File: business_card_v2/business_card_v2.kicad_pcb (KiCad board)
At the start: 2 copper layers, 85.6 x 54 mm, 12 parts, among them M1 CH32X035F7P6, U1 CH32V006F8P6, U10 CH32V006F8P6, U2 CH32V006F8P6, U3 CH32V006F8P6, U4 CH32V006F8P6, U5 CH32V006F8P6, U6 CH32V006F8P6, U7 CH32V006F8P6, U8 CH32V006F8P6, U9 CH32V006F8P6

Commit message: bottom left to top right pins
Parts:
- removed U10: CH32V006F8P6, Package_SO:TSSOP-20_4.4x6.5mm_P0.65mm
- added C1: 100nF, Capacitor_SMD:C_0603_1608Metric, B.Cu at (58.2, 120.0)
- added C10: 10uF, Capacitor_SMD:C_0603_1608Metric, B.Cu at (62.2, 127.5)
- added C11: 100nF, Capacitor_SMD:C_0603_1608Metric, B.Cu at (62.2, 130.0)
- added C12: 100nF, Capacitor_SMD:C_0603_1608Metric, B.Cu at (62.2, 132.5)
- added C13: 100nF, Capacitor_SMD:C_0603_1608Metric, B.Cu at (66.2, 120.0)
- added C14: 100nF, Capacitor_SMD:C_0603_1608Metric, B.Cu at (66.2, 122.5)
- added C15: 100nF, Capacitor_SMD:C_0603_1608Metric, B.Cu at (66.2, 125.0)
- added C16: 100nF, Capacitor_SMD:C_0603_1608Metric, B.Cu at (66.2, 127.5)
- added C17: 100nF, Capacitor_SMD:C_0603_1608Metric, B.Cu at (66.2, 130.0)
- added C18: 100nF, Capacitor_SMD:C_0603_1608Metric, B.Cu at (66.2, 132.5)
- added C19: 100nF, Capacitor_SMD:C_0603_1608Metric, B.Cu at (70.2, 120.0)
- added C2: 100nF, Capacitor_SMD:C_0603_1608Metric, B.Cu at (58.2, 122.5)
- added C20: 100nF, Capacitor_SMD:C_0603_1608Metric, B.Cu at (70.2, 122.5)
- added C21: 100nF, Capacitor_SMD:C_0603_1608Metric, B.Cu at (70.2, 125.0)
- added C22: 100nF, Capacitor_SMD:C_0603_1608Metric, B.Cu at (51.9, 66.7)
- added C23: 100nF, Capacitor_SMD:C_0603_1608Metric, B.Cu at (52.6, 69.1)
- added C26: 100nF, Capacitor_SMD:C_0603_1608Metric, B.Cu at (70.2, 132.5)
- added C3: 100nF, Capacitor_SMD:C_0603_1608Metric, B.Cu at (58.2, 125.0)
- added C4: 100nF, Capacitor_SMD:C_0603_1608Metric, B.Cu at (58.2, 127.5)
- added C5: 100nF, Capacitor_SMD:C_0603_1608Metric, B.Cu at (58.2, 130.0)
- added C6: 100nF, Capacitor_SMD:C_0603_1608Metric, B.Cu at (58.2, 132.5)
- added C7: 10uF, Capacitor_SMD:C_0603_1608Metric, B.Cu at (62.2, 120.0)
- added C8: 100nF, Capacitor_SMD:C_0603_1608Metric, B.Cu at (62.2, 122.5)
- added C9: 100nF, Capacitor_SMD:C_0603_1608Metric, B.Cu at (62.2, 125.0)
- added D1: LED, LED_SMD:LED_1206_3216Metric, B.Cu at (167.9, 126.0)
- added D2: LED, LED_SMD:LED_1206_3216Metric, B.Cu at (168.0, 122.6)
- added D3: LED, LED_SMD:LED_1206_3216Metric, B.Cu at (168.0, 119.2)
- added D4: LED, LED_SMD:LED_1206_3216Metric, B.Cu at (168.0, 115.8)
- added D5: LED, LED_SMD:LED_1206_3216Metric, B.Cu at (168.0, 112.4)
- added D6: LED, LED_SMD:LED_1206_3216Metric, B.Cu at (168.0, 109.0)
- added D7: LED, LED_SMD:LED_1206_3216Metric, B.Cu at (168.0, 105.6)
- added D8: LED, LED_SMD:LED_1206_3216Metric, B.Cu at (168.0, 102.2)
- added D9: LED, LED_SMD:LED_1206_3216Metric, B.Cu at (39.4, 67.7)
- added G***: LOGO, Silkscreen:silkscreen_front_2, F.Cu at (76.9, 65.6)
- added P1: AMS1117-3.3, Package_TO_SOT_SMD:SOT-223-3_TabPin2, B.Cu at (146.9, 100.8)
- added R10: 1k, Resistor_SMD:R_0603_1608Metric, B.Cu at (151.4, 107.8)
- added R11: 1k, Resistor_SMD:R_0603_1608Metric, B.Cu at (41.0, 64.7)
- added R2: 10k, Resistor_SMD:R_0603_1608Metric, B.Cu at (143.9, 111.8)
- added R3: 1k, Resistor_SMD:R_0603_1608Metric, B.Cu at (146.4, 111.8)
- added R4: 1k, Resistor_SMD:R_0603_1608Metric, B.Cu at (148.9, 111.8)
- added R5: 1k, Resistor_SMD:R_0603_1608Metric, B.Cu at (151.4, 111.8)
- added R6: 1k, Resistor_SMD:R_0603_1608Metric, B.Cu at (154.5, 111.8)
- added R7: 1k, Resistor_SMD:R_0603_1608Metric, B.Cu at (143.9, 107.8)
- added R8: 1k, Resistor_SMD:R_0603_1608Metric, B.Cu at (146.4, 107.8)
- added R9: 1k, Resistor_SMD:R_0603_1608Metric, B.Cu at (148.9, 107.8)
- added S1_GP0: ~, TestPoint:TestPoint_Pad_D1.0mm, B.Cu at (111.8, 74.9)
- added S1_GP1: ~, TestPoint:TestPoint_Pad_D1.0mm, B.Cu at (112.4, 77.5)
- added S1_GP10: ~, TestPoint:TestPoint_Pad_D1.0mm, B.Cu at (111.1, 82.5)
- added S1_GP11: ~, TestPoint:TestPoint_Pad_D1.0mm, B.Cu at (110.5, 80.0)
- added S1_GP12: ~, TestPoint:TestPoint_Pad_D1.0mm, B.Cu at (109.9, 77.5)
- added S1_GP13: ~, TestPoint:TestPoint_Pad_D1.0mm, B.Cu at (109.2, 74.9)
- added S1_GP2: ~, TestPoint:TestPoint_Pad_D1.0mm, B.Cu at (113.0, 80.0)
- added S1_GP3: ~, TestPoint:TestPoint_Pad_D1.0mm, B.Cu at (113.7, 82.5)
- added S1_GP4: ~, TestPoint:TestPoint_Pad_D1.0mm, B.Cu at (114.3, 85.1)
- added S1_GP5: ~, TestPoint:TestPoint_Pad_D1.0mm, B.Cu at (114.9, 87.6)
- added S1_GP6: ~, TestPoint:TestPoint_Pad_D1.0mm, B.Cu at (115.6, 90.2)
- added S1_GP7: ~, TestPoint:TestPoint_Pad_D1.0mm, B.Cu at (113.0, 90.2)
- added S1_GP8: ~, TestPoint:TestPoint_Pad_D1.0mm, B.Cu at (112.4, 87.6)
- added S1_GP9: ~, TestPoint:TestPoint_Pad_D1.0mm, B.Cu at (111.8, 85.1)
- added S2_GP0: ~, TestPoint:TestPoint_Pad_D1.0mm, B.Cu at (103.5, 74.9)
- added S2_GP1: ~, TestPoint:TestPoint_Pad_D1.0mm, B.Cu at (104.1, 77.5)
- added S2_GP10: ~, TestPoint:TestPoint_Pad_D1.0mm, B.Cu at (102.9, 82.5)
- added S2_GP11: ~, TestPoint:TestPoint_Pad_D1.0mm, B.Cu at (102.2, 80.0)
- added S2_GP12: ~, TestPoint:TestPoint_Pad_D1.0mm, B.Cu at (101.6, 77.5)
- added S2_GP13: ~, TestPoint:TestPoint_Pad_D1.0mm, B.Cu at (101.0, 74.9)
- added S2_GP2: ~, TestPoint:TestPoint_Pad_D1.0mm, B.Cu at (104.8, 80.0)
- added S2_GP3: ~, TestPoint:TestPoint_Pad_D1.0mm, B.Cu at (105.4, 82.5)
- added S2_GP4: ~, TestPoint:TestPoint_Pad_D1.0mm, B.Cu at (106.0, 85.1)
- added S2_GP5: ~, TestPoint:TestPoint_Pad_D1.0mm, B.Cu at (106.7, 87.6)
- added S2_GP6: ~, TestPoint:TestPoint_Pad_D1.0mm, B.Cu at (107.3, 90.1)
- added S2_GP7: ~, TestPoint:TestPoint_Pad_D1.0mm, B.Cu at (104.8, 90.2)
- added S2_GP8: ~, TestPoint:TestPoint_Pad_D1.0mm, B.Cu at (104.1, 87.6)
- added S2_GP9: ~, TestPoint:TestPoint_Pad_D1.0mm, B.Cu at (103.5, 85.1)
- added S3_GP0: ~, TestPoint:TestPoint_Pad_D1.0mm, B.Cu at (94.6, 74.9)
- added S3_GP1: ~, TestPoint:TestPoint_Pad_D1.0mm, B.Cu at (95.2, 77.5)
- added S3_GP10: ~, TestPoint:TestPoint_Pad_D1.0mm, B.Cu at (94.0, 82.5)
- added S3_GP11: ~, TestPoint:TestPoint_Pad_D1.0mm, B.Cu at (93.3, 80.0)
- added S3_GP12: ~, TestPoint:TestPoint_Pad_D1.0mm, B.Cu at (92.7, 77.5)
- added S3_GP13: ~, TestPoint:TestPoint_Pad_D1.0mm, B.Cu at (92.1, 74.9)
- added S3_GP2: ~, TestPoint:TestPoint_Pad_D1.0mm, B.Cu at (95.9, 80.0)
- added S3_GP3: ~, TestPoint:TestPoint_Pad_D1.0mm, B.Cu at (96.5, 82.5)
- added S3_GP4: ~, TestPoint:TestPoint_Pad_D1.0mm, B.Cu at (97.2, 85.1)
- added S3_GP5: ~, TestPoint:TestPoint_Pad_D1.0mm, B.Cu at (97.8, 87.6)
- added S3_GP6: ~, TestPoint:TestPoint_Pad_D1.0mm, B.Cu at (98.4, 90.2)
- added S3_GP7: ~, TestPoint:TestPoint_Pad_D1.0mm, B.Cu at (95.9, 90.2)
- added S3_GP8: ~, TestPoint:TestPoint_Pad_D1.0mm, B.Cu at (95.2, 87.6)
- added S3_GP9: ~, TestPoint:TestPoint_Pad_D1.0mm, B.Cu at (94.6, 85.1)
- added S4_GP0: ~, TestPoint:TestPoint_Pad_D1.0mm, B.Cu at (85.7, 74.9)
- added S4_GP1: ~, TestPoint:TestPoint_Pad_D1.0mm, B.Cu at (86.4, 77.5)
- added S4_GP10: ~, TestPoint:TestPoint_Pad_D1.0mm, B.Cu at (85.1, 82.5)
- added S4_GP11: ~, TestPoint:TestPoint_Pad_D1.0mm, B.Cu at (84.5, 80.0)
- added S4_GP12: ~, TestPoint:TestPoint_Pad_D1.0mm, B.Cu at (83.8, 77.5)
- added S4_GP13: ~, TestPoint:TestPoint_Pad_D1.0mm, B.Cu at (83.2, 74.9)
- added S4_GP2: ~, TestPoint:TestPoint_Pad_D1.0mm, B.Cu at (87.0, 80.0)
- added S4_GP3: ~, TestPoint:TestPoint_Pad_D1.0mm, B.Cu at (87.6, 82.6)
- added S4_GP4: ~, TestPoint:TestPoint_Pad_D1.0mm, B.Cu at (88.3, 85.1)
- added S4_GP5: ~, TestPoint:TestPoint_Pad_D1.0mm, B.Cu at (88.9, 87.7)
- added S4_GP6: ~, TestPoint:TestPoint_Pad_D1.0mm, B.Cu at (89.5, 90.2)
- added S4_GP7: ~, TestPoint:TestPoint_Pad_D1.0mm, B.Cu at (87.0, 90.2)
- added S4_GP8: ~, TestPoint:TestPoint_Pad_D1.0mm, B.Cu at (86.4, 87.6)
- added S4_GP9: ~, TestPoint:TestPoint_Pad_D1.0mm, B.Cu at (85.7, 85.1)
- added S5_GP0: ~, TestPoint:TestPoint_Pad_D1.0mm, B.Cu at (76.8, 74.9)
- added S5_GP1: ~, TestPoint:TestPoint_Pad_D1.0mm, B.Cu at (77.5, 77.5)
- added S5_GP10: ~, TestPoint:TestPoint_Pad_D1.0mm, B.Cu at (76.2, 82.5)
- added S5_GP11: ~, TestPoint:TestPoint_Pad_D1.0mm, B.Cu at (75.6, 80.0)
- added S5_GP12: ~, TestPoint:TestPoint_Pad_D1.0mm, B.Cu at (74.9, 77.5)
- added S5_GP13: ~, TestPoint:TestPoint_Pad_D1.0mm, B.Cu at (74.3, 74.9)
- added S5_GP2: ~, TestPoint:TestPoint_Pad_D1.0mm, B.Cu at (78.1, 80.0)
- added S5_GP3: ~, TestPoint:TestPoint_Pad_D1.0mm, B.Cu at (78.7, 82.5)
- added S5_GP4: ~, TestPoint:TestPoint_Pad_D1.0mm, B.Cu at (79.4, 85.1)
- added S5_GP5: ~, TestPoint:TestPoint_Pad_D1.0mm, B.Cu at (80.0, 87.6)
- added S5_GP6: ~, TestPoint:TestPoint_Pad_D1.0mm, B.Cu at (80.6, 90.2)
- added S5_GP7: ~, TestPoint:TestPoint_Pad_D1.0mm, B.Cu at (78.1, 90.2)
- added S5_GP8: ~, TestPoint:TestPoint_Pad_D1.0mm, B.Cu at (77.5, 87.6)
- added S5_GP9: ~, TestPoint:TestPoint_Pad_D1.0mm, B.Cu at (76.8, 85.1)
- added S6_GP0: ~, TestPoint:TestPoint_Pad_D1.0mm, B.Cu at (67.9, 74.9)
- added S6_GP1: ~, TestPoint:TestPoint_Pad_D1.0mm, B.Cu at (68.6, 77.5)
- added S6_GP10: ~, TestPoint:TestPoint_Pad_D1.0mm, B.Cu at (67.3, 82.5)
- added S6_GP11: ~, TestPoint:TestPoint_Pad_D1.0mm, B.Cu at (66.7, 80.0)
- added S6_GP12: ~, TestPoint:TestPoint_Pad_D1.0mm, B.Cu at (66.0, 77.5)
- added S6_GP13: ~, TestPoint:TestPoint_Pad_D1.0mm, B.Cu at (65.4, 74.9)
- added S6_GP2: ~, TestPoint:TestPoint_Pad_D1.0mm, B.Cu at (69.2, 80.0)
- added S6_GP3: ~, TestPoint:TestPoint_Pad_D1.0mm, B.Cu at (69.8, 82.5)
- added S6_GP4: ~, TestPoint:TestPoint_Pad_D1.0mm, B.Cu at (70.5, 85.1)
- added S6_GP5: ~, TestPoint:TestPoint_Pad_D1.0mm, B.Cu at (71.1, 87.6)
- added S6_GP6: ~, TestPoint:TestPoint_Pad_D1.0mm, B.Cu at (71.8, 90.2)
- added S6_GP7: ~, TestPoint:TestPoint_Pad_D1.0mm, B.Cu at (69.2, 90.2)
- added S6_GP8: ~, TestPoint:TestPoint_Pad_D1.0mm, B.Cu at (68.6, 87.6)
- added S6_GP9: ~, TestPoint:TestPoint_Pad_D1.0mm, B.Cu at (67.9, 85.1)
- added S7_GP0: ~, TestPoint:TestPoint_Pad_D1.0mm, B.Cu at (59.1, 74.9)
- added S7_GP1: ~, TestPoint:TestPoint_Pad_D1.0mm, B.Cu at (59.7, 77.5)
- added S7_GP10: ~, TestPoint:TestPoint_Pad_D1.0mm, B.Cu at (58.4, 82.5)
- added S7_GP11: ~, TestPoint:TestPoint_Pad_D1.0mm, B.Cu at (57.8, 80.0)
- added S7_GP12: ~, TestPoint:TestPoint_Pad_D1.0mm, B.Cu at (57.1, 77.5)
- added S7_GP13: ~, TestPoint:TestPoint_Pad_D1.0mm, B.Cu at (56.5, 74.9)
- added S7_GP2: ~, TestPoint:TestPoint_Pad_D1.0mm, B.Cu at (61.6, 85.1)
- added S7_GP3: ~, TestPoint:TestPoint_Pad_D1.0mm, B.Cu at (60.3, 80.0)
- added S7_GP4: ~, TestPoint:TestPoint_Pad_D1.0mm, B.Cu at (61.0, 82.5)
- added S7_GP5: ~, TestPoint:TestPoint_Pad_D1.0mm, B.Cu at (62.2, 87.6)
- added S7_GP6: ~, TestPoint:TestPoint_Pad_D1.0mm, B.Cu at (62.9, 90.2)
- added S7_GP7: ~, TestPoint:TestPoint_Pad_D1.0mm, B.Cu at (60.3, 90.2)
- added S7_GP8: ~, TestPoint:TestPoint_Pad_D1.0mm, B.Cu at (59.7, 87.6)
- added S7_GP9: ~, TestPoint:TestPoint_Pad_D1.0mm, B.Cu at (59.1, 85.1)
- added S8_GP0: ~, TestPoint:TestPoint_Pad_D1.0mm, B.Cu at (50.2, 74.9)
- added S8_GP1: ~, TestPoint:TestPoint_Pad_D1.0mm, B.Cu at (50.8, 77.5)
- added S8_GP10: ~, TestPoint:TestPoint_Pad_D1.0mm, B.Cu at (49.5, 82.5)
- added S8_GP11: ~, TestPoint:TestPoint_Pad_D1.0mm, B.Cu at (48.9, 80.0)
- added S8_GP12: ~, TestPoint:TestPoint_Pad_D1.0mm, B.Cu at (48.3, 77.5)
- added S8_GP13: ~, TestPoint:TestPoint_Pad_D1.0mm, B.Cu at (47.6, 74.9)
- added S8_GP2: ~, TestPoint:TestPoint_Pad_D1.0mm, B.Cu at (51.4, 80.0)
- added S8_GP3: ~, TestPoint:TestPoint_Pad_D1.0mm, B.Cu at (52.1, 82.5)
- added S8_GP4: ~, TestPoint:TestPoint_Pad_D1.0mm, B.Cu at (52.7, 85.1)
- added S8_GP5: ~, TestPoint:TestPoint_Pad_D1.0mm, B.Cu at (53.3, 87.6)
- added S8_GP6: ~, TestPoint:TestPoint_Pad_D1.0mm, B.Cu at (54.0, 90.2)
- added S8_GP7: ~, TestPoint:TestPoint_Pad_D1.0mm, B.Cu at (51.4, 90.2)
- added S8_GP8: ~, TestPoint:TestPoint_Pad_D1.0mm, B.Cu at (50.8, 87.6)
- added S8_GP9: ~, TestPoint:TestPoint_Pad_D1.0mm, B.Cu at (50.2, 85.1)
- added S9_GP0: ~, TestPoint:TestPoint_Pad_D1.0mm, B.Cu at (41.3, 74.9)
- added S9_GP1: ~, TestPoint:TestPoint_Pad_D1.0mm, B.Cu at (41.9, 77.5)
- added S9_GP10: ~, TestPoint:TestPoint_Pad_D1.0mm, B.Cu at (40.6, 82.5)
- added S9_GP11: ~, TestPoint:TestPoint_Pad_D1.0mm, B.Cu at (40.0, 80.0)
- added S9_GP12: ~, TestPoint:TestPoint_Pad_D1.0mm, B.Cu at (39.4, 77.5)
- added S9_GP13: ~, TestPoint:TestPoint_Pad_D1.0mm, B.Cu at (38.7, 74.9)
- added S9_GP2: ~, TestPoint:TestPoint_Pad_D1.0mm, B.Cu at (42.5, 80.0)
- added S9_GP3: ~, TestPoint:TestPoint_Pad_D1.0mm, B.Cu at (43.2, 82.5)
- added S9_GP4: ~, TestPoint:TestPoint_Pad_D1.0mm, B.Cu at (43.8, 85.1)
- added S9_GP5: ~, TestPoint:TestPoint_Pad_D1.0mm, B.Cu at (44.5, 87.6)
- added S9_GP6: ~, TestPoint:TestPoint_Pad_D1.0mm, B.Cu at (45.1, 90.2)
- added S9_GP7: ~, TestPoint:TestPoint_Pad_D1.0mm, B.Cu at (42.5, 90.2)
- added S9_GP8: ~, TestPoint:TestPoint_Pad_D1.0mm, B.Cu at (41.9, 87.6)
- added S9_GP9: ~, TestPoint:TestPoint_Pad_D1.0mm, B.Cu at (41.3, 85.1)
- added SW3: SW_Push, Button_Switch_SMD:SW_SPST_TL3342, B.Cu at (154.5, 101.0)
- added TP1: SWIO_N1, TestPoint:TestPoint_Pad_D2.0mm, B.Cu at (116.8, 67.3)
- added TP11: SWDIO_M, TestPoint:TestPoint_Pad_D2.0mm, B.Cu at (113.7, 59.7)
- added TP12: SWCLK_M, TestPoint:TestPoint_Pad_D2.0mm, B.Cu at (113.7, 63.5)
- added TP13: GND, TestPoint:TestPoint_Pad_D2.0mm, B.Cu at (116.8, 59.7)
- added TP14: BUS_MOSI, TestPoint:TestPoint_Pad_D2.0mm, B.Cu at (110.5, 59.7)
- added TP15: BUS_MISO, TestPoint:TestPoint_Pad_D2.0mm, B.Cu at (110.5, 63.5)
- added TP2: SWIO_N2, TestPoint:TestPoint_Pad_D2.0mm, B.Cu at (116.8, 71.1)
- added TP3: SWIO_N3, TestPoint:TestPoint_Pad_D2.0mm, B.Cu at (113.7, 67.3)
- added TP4: SWIO_N4, TestPoint:TestPoint_Pad_D2.0mm, B.Cu at (113.7, 71.1)
- added TP5: SWIO_N5, TestPoint:TestPoint_Pad_D2.0mm, B.Cu at (110.5, 67.3)
- added TP6: SWIO_N6, TestPoint:TestPoint_Pad_D2.0mm, B.Cu at (110.5, 71.1)
- added TP7: SWIO_N7, TestPoint:TestPoint_Pad_D2.0mm, B.Cu at (107.3, 67.3)
- added TP8: SWIO_N8, TestPoint:TestPoint_Pad_D2.0mm, B.Cu at (107.3, 71.1)
- added TP9: SWIO_N9, TestPoint:TestPoint_Pad_D2.0mm, B.Cu at (116.8, 74.9)
- M1, U1, U2, U3, U4, U5, U6, U7, U8, U9: moved to B.Cu
- moved U7 48.1 mm to (46.4, 44.5), turned to 180 degrees
- moved U9 44.4 mm to (46.4, 67.3), turned to 180 degrees
- moved U8 44.1 mm to (46.4, 55.9), turned to 180 degrees
- moved M1 34.6 mm to (106.5, 49.5)
- moved J1 27.0 mm to (113.4, 50.8)
- moved U1 23.2 mm to (95.2, 63.5), turned to 180 degrees
- moved U2 22.0 mm to (81.5, 49.5), turned to 180 degrees
- moved U4 17.1 mm to (66.7, 44.5), turned to 180 degrees
- moved U3 16.9 mm to (81.5, 63.5), turned to 180 degrees
- moved U5 15.7 mm to (66.6, 55.9), turned to 180 degrees
- moved U6 14.7 mm to (66.7, 67.3), turned to 180 degrees
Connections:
- J1 pad A1: unconnected-(J1-GND-PadA1) -> GND
- J1 pad A12: unconnected-(J1-GND-PadA12) -> GND
- J1 pad A4: unconnected-(J1-VBUS-PadA4) -> +5V
- J1 pad A5: unconnected-(J1-CC1-PadA5) -> /CC1
- J1 pad A6: unconnected-(J1-DP1-PadA6) -> /D+
- J1 pad A7: unconnected-(J1-DN1-PadA7) -> /D-
- J1 pad A9: unconnected-(J1-VBUS-PadA9) -> +5V
- J1 pad B1: unconnected-(J1-GND-PadB1) -> GND
- J1 pad B12: unconnected-(J1-GND-PadB12) -> GND
- J1 pad B4: unconnected-(J1-VBUS-PadB4) -> +5V
- J1 pad B6: unconnected-(J1-DP2-PadB6) -> /D+
- J1 pad B7: unconnected-(J1-DN2-PadB7) -> /D-
- J1 pad B9: unconnected-(J1-VBUS-PadB9) -> +5V
- M1 pad 1: unconnected-(M1-PB12-Pad1) -> /NRST_S1
- M1 pad 10: unconnected-(M1-PA4-Pad10) -> /NRST_S5
- M1 pad 11: unconnected-(M1-PA5-Pad11) -> /NRST_S6
- M1 pad 12: unconnected-(M1-PA6-Pad12) -> /NRST_S7
- M1 pad 13: unconnected-(M1-PA7-Pad13) -> /NRST_S8
- M1 pad 14: unconnected-(M1-PB1-Pad14) -> /NRST_S9
- M1 pad 15: unconnected-(M1-GND-Pad15) -> GND
- M1 pad 16: unconnected-(M1-VDD-Pad16) -> +3.3V
- M1 pad 17: unconnected-(M1-PC16-Pad17) -> /D+
- M1 pad 18: unconnected-(M1-PC17-Pad18) -> /D-
- M1 pad 19: unconnected-(M1-PC18-Pad19) -> /SWDIO_M
- M1 pad 2: unconnected-(M1-PC14-Pad2) -> /CC1
- M1 pad 20: unconnected-(M1-PC19-Pad20) -> /SWCLK_M
- M1 pad 4: unconnected-(M1-PC3-Pad4) -> /NRST_MASTER
- M1 pad 5: unconnected-(M1-PC1-Pad5) -> /NRST_S2
- M1 pad 6: unconnected-(M1-PA0-Pad6) -> /NRST_S3
- M1 pad 7: unconnected-(M1-PA1-Pad7) -> /NRST_S4
- M1 pad 8: unconnected-(M1-PA2-Pad8) -> /BUS_MOSI
- M1 pad 9: unconnected-(M1-PA3-Pad9) -> /BUS_MISO
- U1 pad 1: unconnected-(U1-PD4-Pad1) -> Net-(U1-PD4)
- U1 pad 10: unconnected-(U1-PC0-Pad10) -> Net-(U1-PC0)
- U1 pad 11: unconnected-(U1-PC1-Pad11) -> Net-(U1-PC1)
- U1 pad 12: unconnected-(U1-PC2-Pad12) -> Net-(U1-PC2)
- U1 pad 13: unconnected-(U1-PC3-Pad13) -> Net-(U1-PC3)
- U1 pad 14: unconnected-(U1-PC4-Pad14) -> Net-(U1-PC4)
- U1 pad 15: unconnected-(U1-PC5-Pad15) -> Net-(U1-PC5)
- U1 pad 16: unconnected-(U1-PC6-Pad16) -> Net-(U1-PC6)
- U1 pad 17: unconnected-(U1-PC7-Pad17) -> Net-(U1-PC7)
- U1 pad 18: unconnected-(U1-PD1-Pad18) -> /SWIO_N1
- U1 pad 19: unconnected-(U1-PD2-Pad19) -> Net-(U1-PD2)
- U1 pad 2: unconnected-(U1-PD5-Pad2) -> /BUS_MISO
- U1 pad 20: unconnected-(U1-PD3-Pad20) -> Net-(U1-PD3)
- U1 pad 3: unconnected-(U1-PD6-Pad3) -> /BUS_MOSI
- U1 pad 4: unconnected-(U1-PD7-Pad4) -> /NRST_S1
- U1 pad 5: unconnected-(U1-PA1-Pad5) -> Net-(U1-PA1)
- U1 pad 6: unconnected-(U1-PA2-Pad6) -> Net-(U1-PA2)
- U1 pad 7: unconnected-(U1-VSS-Pad7) -> GND
- U1 pad 8: unconnected-(U1-PD0-Pad8) -> Net-(U1-PD0)
- U1 pad 9: unconnected-(U1-VDD-Pad9) -> +3.3V
- U2 pad 1: unconnected-(U2-PD4-Pad1) -> Net-(U2-PD4)
- U2 pad 10: unconnected-(U2-PC0-Pad10) -> Net-(U2-PC0)
- U2 pad 11: unconnected-(U2-PC1-Pad11) -> Net-(U2-PC1)
- U2 pad 12: unconnected-(U2-PC2-Pad12) -> Net-(U2-PC2)
- U2 pad 13: unconnected-(U2-PC3-Pad13) -> Net-(U2-PC3)
- U2 pad 14: unconnected-(U2-PC4-Pad14) -> Net-(U2-PC4)
- U2 pad 15: unconnected-(U2-PC5-Pad15) -> Net-(U2-PC5)
- U2 pad 16: unconnected-(U2-PC6-Pad16) -> Net-(U2-PC6)
- U2 pad 17: unconnected-(U2-PC7-Pad17) -> Net-(U2-PC7)
- U2 pad 18: unconnected-(U2-PD1-Pad18) -> /SWIO_N2
- U2 pad 19: unconnected-(U2-PD2-Pad19) -> Net-(U2-PD2)
- U2 pad 2: unconnected-(U2-PD5-Pad2) -> /BUS_MISO
- U2 pad 20: unconnected-(U2-PD3-Pad20) -> Net-(U2-PD3)
- U2 pad 3: unconnected-(U2-PD6-Pad3) -> /BUS_MOSI
- U2 pad 4: unconnected-(U2-PD7-Pad4) -> /NRST_S2
- U2 pad 5: unconnected-(U2-PA1-Pad5) -> Net-(U2-PA1)
- U2 pad 6: unconnected-(U2-PA2-Pad6) -> Net-(U2-PA2)
- U2 pad 7: unconnected-(U2-VSS-Pad7) -> GND
- U2 pad 8: unconnected-(U2-PD0-Pad8) -> Net-(U2-PD0)
- U2 pad 9: unconnected-(U2-VDD-Pad9) -> +3.3V
- U3 pad 1: unconnected-(U3-PD4-Pad1) -> Net-(U3-PD4)
- U3 pad 10: unconnected-(U3-PC0-Pad10) -> Net-(U3-PC0)
- U3 pad 11: unconnected-(U3-PC1-Pad11) -> Net-(U3-PC1)
- U3 pad 12: unconnected-(U3-PC2-Pad12) -> Net-(U3-PC2)
- U3 pad 13: unconnected-(U3-PC3-Pad13) -> Net-(U3-PC3)
- U3 pad 14: unconnected-(U3-PC4-Pad14) -> Net-(U3-PC4)
- U3 pad 15: unconnected-(U3-PC5-Pad15) -> Net-(U3-PC5)
- U3 pad 16: unconnected-(U3-PC6-Pad16) -> Net-(U3-PC6)
- U3 pad 17: unconnected-(U3-PC7-Pad17) -> Net-(U3-PC7)
- U3 pad 18: unconnected-(U3-PD1-Pad18) -> /SWIO_N3
- U3 pad 19: unconnected-(U3-PD2-Pad19) -> Net-(U3-PD2)
- U3 pad 2: unconnected-(U3-PD5-Pad2) -> /BUS_MISO
- U3 pad 20: unconnected-(U3-PD3-Pad20) -> Net-(U3-PD3)
- U3 pad 3: unconnected-(U3-PD6-Pad3) -> /BUS_MOSI
- U3 pad 4: unconnected-(U3-PD7-Pad4) -> /NRST_S3
- U3 pad 5: unconnected-(U3-PA1-Pad5) -> Net-(U3-PA1)
- U3 pad 6: unconnected-(U3-PA2-Pad6) -> Net-(U3-PA2)
- U3 pad 7: unconnected-(U3-VSS-Pad7) -> GND
- U3 pad 8: unconnected-(U3-PD0-Pad8) -> Net-(U3-PD0)
- U3 pad 9: unconnected-(U3-VDD-Pad9) -> +3.3V
- U4 pad 1: unconnected-(U4-PD4-Pad1) -> Net-(U4-PD4)
- U4 pad 10: unconnected-(U4-PC0-Pad10) -> Net-(U4-PC0)
- U4 pad 11: unconnected-(U4-PC1-Pad11) -> Net-(U4-PC1)
- U4 pad 12: unconnected-(U4-PC2-Pad12) -> Net-(U4-PC2)
- U4 pad 13: unconnected-(U4-PC3-Pad13) -> Net-(U4-PC3)
- U4 pad 14: unconnected-(U4-PC4-Pad14) -> Net-(U4-PC4)
- U4 pad 15: unconnected-(U4-PC5-Pad15) -> Net-(U4-PC5)
- U4 pad 16: unconnected-(U4-PC6-Pad16) -> Net-(U4-PC6)
- U4 pad 17: unconnected-(U4-PC7-Pad17) -> Net-(U4-PC7)
- U4 pad 18: unconnected-(U4-PD1-Pad18) -> /SWIO_N4
- U4 pad 19: unconnected-(U4-PD2-Pad19) -> Net-(U4-PD2)
- U4 pad 2: unconnected-(U4-PD5-Pad2) -> /BUS_MISO
- U4 pad 20: unconnected-(U4-PD3-Pad20) -> Net-(U4-PD3)
- U4 pad 3: unconnected-(U4-PD6-Pad3) -> /BUS_MOSI
- U4 pad 4: unconnected-(U4-PD7-Pad4) -> /NRST_S4
- U4 pad 5: unconnected-(U4-PA1-Pad5) -> Net-(U4-PA1)
- U4 pad 6: unconnected-(U4-PA2-Pad6) -> Net-(U4-PA2)
- U4 pad 7: unconnected-(U4-VSS-Pad7) -> GND
- U4 pad 8: unconnected-(U4-PD0-Pad8) -> Net-(U4-PD0)
- U4 pad 9: unconnected-(U4-VDD-Pad9) -> +3.3V
- U5 pad 1: unconnected-(U5-PD4-Pad1) -> Net-(U5-PD4)
- U5 pad 10: unconnected-(U5-PC0-Pad10) -> Net-(U5-PC0)
- U5 pad 11: unconnected-(U5-PC1-Pad11) -> Net-(U5-PC1)
- U5 pad 12: unconnected-(U5-PC2-Pad12) -> Net-(U5-PC2)
- U5 pad 13: unconnected-(U5-PC3-Pad13) -> Net-(U5-PC3)
- U5 pad 14: unconnected-(U5-PC4-Pad14) -> Net-(U5-PC4)
- U5 pad 15: unconnected-(U5-PC5-Pad15) -> Net-(U5-PC5)
- U5 pad 16: unconnected-(U5-PC6-Pad16) -> Net-(U5-PC6)
- U5 pad 17: unconnected-(U5-PC7-Pad17) -> Net-(U5-PC7)
- U5 pad 18: unconnected-(U5-PD1-Pad18) -> /SWIO_N5
- U5 pad 19: unconnected-(U5-PD2-Pad19) -> Net-(U5-PD2)
- U5 pad 2: unconnected-(U5-PD5-Pad2) -> /BUS_MISO
- U5 pad 20: unconnected-(U5-PD3-Pad20) -> Net-(U5-PD3)
- U5 pad 3: unconnected-(U5-PD6-Pad3) -> /BUS_MOSI
- U5 pad 4: unconnected-(U5-PD7-Pad4) -> /NRST_S5
- U5 pad 5: unconnected-(U5-PA1-Pad5) -> Net-(U5-PA1)
- U5 pad 6: unconnected-(U5-PA2-Pad6) -> Net-(U5-PA2)
- U5 pad 7: unconnected-(U5-VSS-Pad7) -> GND
- U5 pad 8: unconnected-(U5-PD0-Pad8) -> Net-(U5-PD0)
- U5 pad 9: unconnected-(U5-VDD-Pad9) -> +3.3V
- U6 pad 1: unconnected-(U6-PD4-Pad1) -> Net-(U6-PD4)
- U6 pad 10: unconnected-(U6-PC0-Pad10) -> Net-(U6-PC0)
- U6 pad 11: unconnected-(U6-PC1-Pad11) -> Net-(U6-PC1)
- U6 pad 12: unconnected-(U6-PC2-Pad12) -> Net-(U6-PC2)
- U6 pad 13: unconnected-(U6-PC3-Pad13) -> Net-(U6-PC3)
- U6 pad 14: unconnected-(U6-PC4-Pad14) -> Net-(U6-PC4)
- U6 pad 15: unconnected-(U6-PC5-Pad15) -> Net-(U6-PC5)
- U6 pad 16: unconnected-(U6-PC6-Pad16) -> Net-(U6-PC6)
- U6 pad 17: unconnected-(U6-PC7-Pad17) -> Net-(U6-PC7)
- U6 pad 18: unconnected-(U6-PD1-Pad18) -> /SWIO_N6
- U6 pad 19: unconnected-(U6-PD2-Pad19) -> Net-(U6-PD2)
- U6 pad 2: unconnected-(U6-PD5-Pad2) -> /BUS_MISO
- U6 pad 20: unconnected-(U6-PD3-Pad20) -> Net-(U6-PD3)
- U6 pad 3: unconnected-(U6-PD6-Pad3) -> /BUS_MOSI
- U6 pad 4: unconnected-(U6-PD7-Pad4) -> /NRST_S6
- U6 pad 5: unconnected-(U6-PA1-Pad5) -> Net-(U6-PA1)
- U6 pad 6: unconnected-(U6-PA2-Pad6) -> Net-(U6-PA2)
- U6 pad 7: unconnected-(U6-VSS-Pad7) -> GND
- U6 pad 8: unconnected-(U6-PD0-Pad8) -> Net-(U6-PD0)
- U6 pad 9: unconnected-(U6-VDD-Pad9) -> +3.3V
- U7 pad 1: unconnected-(U7-PD4-Pad1) -> Net-(U7-PD4)
- U7 pad 10: unconnected-(U7-PC0-Pad10) -> Net-(U7-PC0)
- U7 pad 11: unconnected-(U7-PC1-Pad11) -> Net-(U7-PC1)
- U7 pad 12: unconnected-(U7-PC2-Pad12) -> Net-(U7-PC2)
- U7 pad 13: unconnected-(U7-PC3-Pad13) -> Net-(U7-PC3)
- U7 pad 14: unconnected-(U7-PC4-Pad14) -> Net-(U7-PC4)
- U7 pad 15: unconnected-(U7-PC5-Pad15) -> Net-(U7-PC5)
- U7 pad 16: unconnected-(U7-PC6-Pad16) -> Net-(U7-PC6)
- U7 pad 17: unconnected-(U7-PC7-Pad17) -> Net-(U7-PC7)
- U7 pad 18: unconnected-(U7-PD1-Pad18) -> /SWIO_N7
- U7 pad 19: unconnected-(U7-PD2-Pad19) -> Net-(U7-PD2)
- U7 pad 2: unconnected-(U7-PD5-Pad2) -> /BUS_MISO
- U7 pad 20: unconnected-(U7-PD3-Pad20) -> Net-(U7-PD3)
- U7 pad 3: unconnected-(U7-PD6-Pad3) -> /BUS_MOSI
- U7 pad 4: unconnected-(U7-PD7-Pad4) -> /NRST_S7
- U7 pad 5: unconnected-(U7-PA1-Pad5) -> Net-(U7-PA1)
- U7 pad 6: unconnected-(U7-PA2-Pad6) -> Net-(U7-PA2)
- U7 pad 7: unconnected-(U7-VSS-Pad7) -> GND
- U7 pad 8: unconnected-(U7-PD0-Pad8) -> Net-(U7-PD0)
- U7 pad 9: unconnected-(U7-VDD-Pad9) -> +3.3V
- U8 pad 1: unconnected-(U8-PD4-Pad1) -> Net-(U8-PD4)
- U8 pad 10: unconnected-(U8-PC0-Pad10) -> Net-(U8-PC0)
- U8 pad 11: unconnected-(U8-PC1-Pad11) -> Net-(U8-PC1)
- U8 pad 12: unconnected-(U8-PC2-Pad12) -> Net-(U8-PC2)
- U8 pad 13: unconnected-(U8-PC3-Pad13) -> Net-(U8-PC3)
- U8 pad 14: unconnected-(U8-PC4-Pad14) -> Net-(U8-PC4)
- U8 pad 15: unconnected-(U8-PC5-Pad15) -> Net-(U8-PC5)
- U8 pad 16: unconnected-(U8-PC6-Pad16) -> Net-(U8-PC6)
- U8 pad 17: unconnected-(U8-PC7-Pad17) -> Net-(U8-PC7)
- U8 pad 18: unconnected-(U8-PD1-Pad18) -> /SWIO_N8
- U8 pad 19: unconnected-(U8-PD2-Pad19) -> Net-(U8-PD2)
- U8 pad 2: unconnected-(U8-PD5-Pad2) -> /BUS_MISO
- U8 pad 20: unconnected-(U8-PD3-Pad20) -> Net-(U8-PD3)
- U8 pad 3: unconnected-(U8-PD6-Pad3) -> /BUS_MOSI
- U8 pad 4: unconnected-(U8-PD7-Pad4) -> /NRST_S8
- U8 pad 5: unconnected-(U8-PA1-Pad5) -> Net-(U8-PA1)
- U8 pad 6: unconnected-(U8-PA2-Pad6) -> Net-(U8-PA2)
- U8 pad 7: unconnected-(U8-VSS-Pad7) -> GND
- U8 pad 8: unconnected-(U8-PD0-Pad8) -> Net-(U8-PD0)
- U8 pad 9: unconnected-(U8-VDD-Pad9) -> +3.3V
- U9 pad 1: unconnected-(U9-PD4-Pad1) -> Net-(U9-PD4)
- U9 pad 10: unconnected-(U9-PC0-Pad10) -> Net-(U9-PC0)
- U9 pad 11: unconnected-(U9-PC1-Pad11) -> Net-(U9-PC1)
- U9 pad 12: unconnected-(U9-PC2-Pad12) -> Net-(U9-PC2)
- U9 pad 13: unconnected-(U9-PC3-Pad13) -> Net-(U9-PC3)
- U9 pad 14: unconnected-(U9-PC4-Pad14) -> Net-(U9-PC4)
- U9 pad 15: unconnected-(U9-PC5-Pad15) -> Net-(U9-PC5)
- U9 pad 16: unconnected-(U9-PC6-Pad16) -> Net-(U9-PC6)
- U9 pad 17: unconnected-(U9-PC7-Pad17) -> Net-(U9-PC7)
- U9 pad 18: unconnected-(U9-PD1-Pad18) -> /SWIO_N9
- U9 pad 19: unconnected-(U9-PD2-Pad19) -> Net-(U9-PD2)
- U9 pad 2: unconnected-(U9-PD5-Pad2) -> /BUS_MISO
- U9 pad 20: unconnected-(U9-PD3-Pad20) -> Net-(U9-PD3)
- U9 pad 3: unconnected-(U9-PD6-Pad3) -> /BUS_MOSI
- U9 pad 4: unconnected-(U9-PD7-Pad4) -> /NRST_S9
- U9 pad 5: unconnected-(U9-PA1-Pad5) -> Net-(U9-PA1)
- U9 pad 6: unconnected-(U9-PA2-Pad6) -> Net-(U9-PA2)
- U9 pad 7: unconnected-(U9-VSS-Pad7) -> GND
- U9 pad 8: unconnected-(U9-PD0-Pad8) -> Net-(U9-PD0)
- U9 pad 9: unconnected-(U9-VDD-Pad9) -> +3.3V
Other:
- outline, holes or cut-outs redrawn

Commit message: 9 S1 pins pattern
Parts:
- moved C10 85.3 mm to (107.5, 55.2)
- moved C7 85.3 mm to (107.5, 47.7)
- moved C9 85.3 mm to (107.5, 52.7)
- moved C8 85.3 mm to (107.5, 50.2)
- moved P1 73.1 mm to (100.3, 44.5)
- moved SW3 71.3 mm to (113.7, 42.5), turned to 0 degrees
- moved U1 20.8 mm to (87.0, 44.5)
- moved TP15 13.6 mm to (116.8, 75.6)
- moved TP14 13.1 mm to (116.8, 71.1)
- moved TP9 13.1 mm to (105.4, 68.6)
- moved TP4 12.9 mm to (109.2, 59.1)
- moved M1 12.0 mm to (97.8, 57.8)
- moved TP1 9.67 mm to (113.0, 58.4)
- moved TP2 9.09 mm to (113.0, 62.9)
- moved U2 8.45 mm to (87.0, 55.9)
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
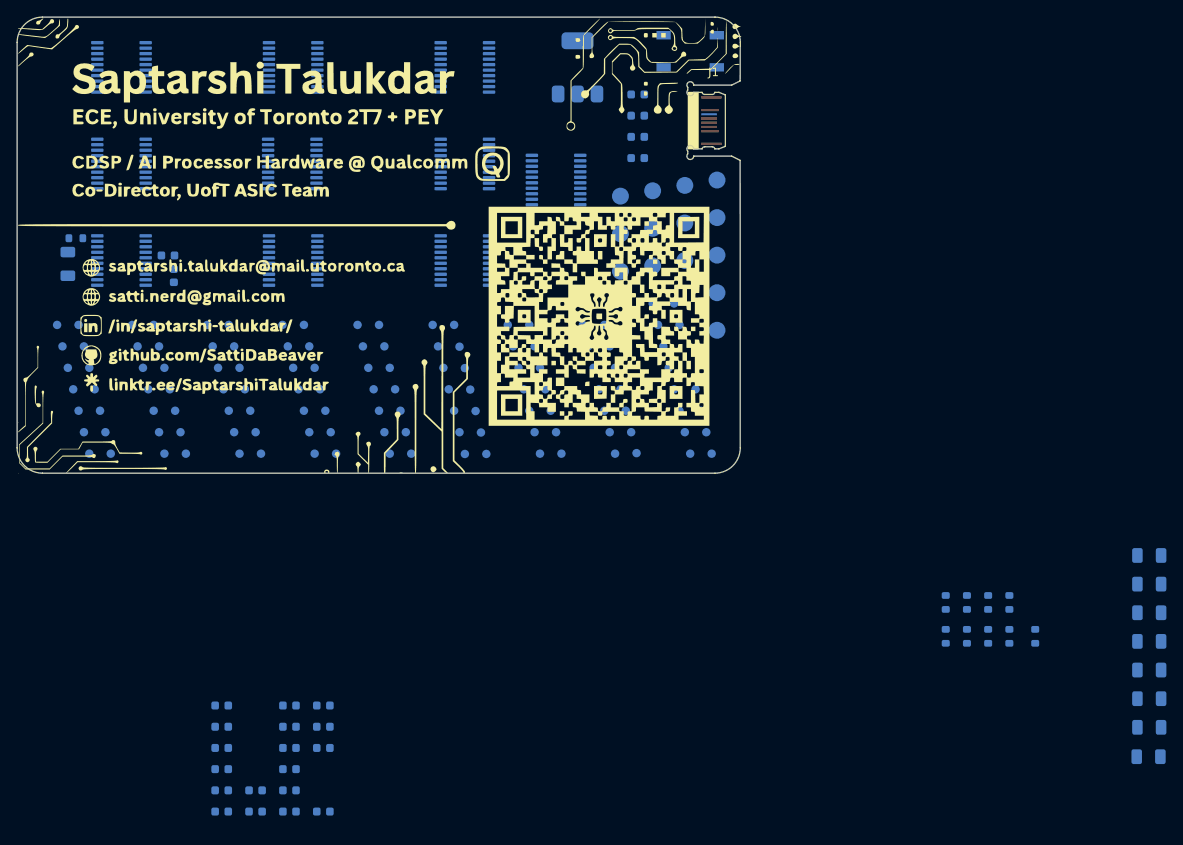
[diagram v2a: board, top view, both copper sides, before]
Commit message: added basic traces
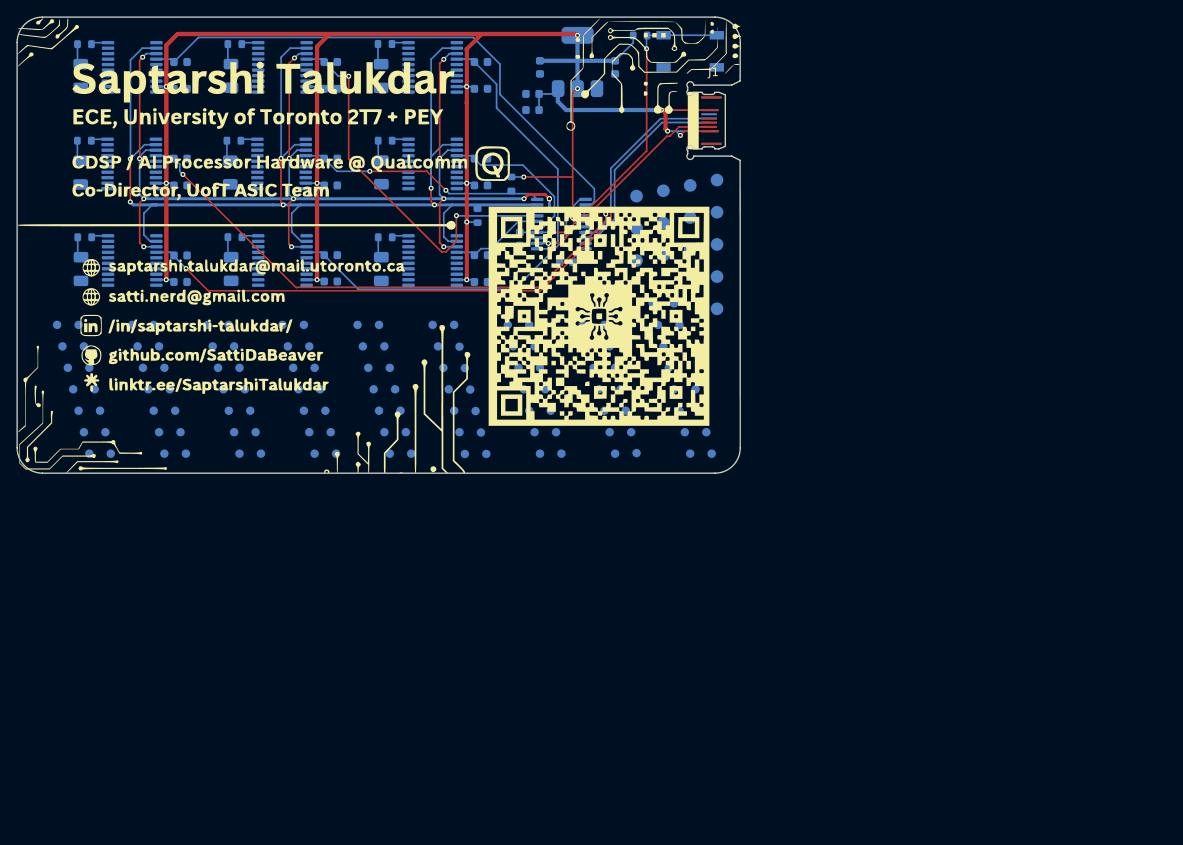
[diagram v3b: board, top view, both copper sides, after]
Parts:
- added R12: 5.1k, Resistor_SMD:R_0603_1608Metric, B.Cu at (92.5, 58.2)
- added R13: 5.1k, Resistor_SMD:R_0603_1608Metric, B.Cu at (88.5, 62.0)
- TP1, TP11, TP12, TP13, TP14, TP15, TP2, TP3, TP4, TP5, TP6, TP7, TP8, TP9: footprint TestPoint:TestPoint_Pad_D2.0mm -> TestPoint:TestPoint_Pad_D1.5mm
- moved D7 140.0 mm to (41.5, 45.5), turned to 90 degrees
- moved D8 134.4 mm to (41.5, 56.9), turned to 90 degrees
- moved D4 129.4 mm to (59.3, 45.5), turned to 90 degrees
- moved R9 125.7 mm to (42.0, 41.7), turned to 180 degrees
- moved R10 122.4 mm to (42.0, 53.1), turned to 180 degrees
- moved D5 122.1 mm to (59.2, 56.9), turned to 90 degrees
- moved D1 121.4 mm to (77.1, 45.5), turned to 90 degrees
- moved R6 117.8 mm to (59.8, 41.7), turned to 180 degrees
- moved D6 116.0 mm to (59.3, 68.3), turned to 90 degrees
- moved D2 112.1 mm to (77.1, 56.9), turned to 90 degrees
- moved D3 104.2 mm to (77.1, 68.3), turned to 90 degrees
- moved R7 100.4 mm to (59.7, 53.1), turned to 180 degrees
- moved R3 98.3 mm to (77.5, 41.7), turned to 180 degrees
- moved R8 96.8 mm to (59.8, 64.5), turned to 180 degrees
- moved R4 92.4 mm to (77.6, 53.1), turned to 180 degrees
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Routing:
- net +3.3V: track 0.00 -> 201.7 mm, vias 0 -> 14
- net /BUS_MISO: track 0.00 -> 148.0 mm, vias 0 -> 6
- net /BUS_MOSI: track 0.00 -> 138.1 mm, vias 0 -> 15
- net /NRST_S8: track 0.00 -> 66.7 mm, vias 0 -> 2
- net /NRST_S7: track 0.00 -> 65.4 mm
- net /NRST_S9: track 0.00 -> 63.7 mm, vias 0 -> 2
- net /NRST_S4: track 0.00 -> 46.0 mm, vias 0 -> 2
- net +5V: track 0.00 -> 42.6 mm, vias 0 -> 3
- net /NRST_MASTER: track 0.00 -> 41.0 mm, vias 0 -> 2
- net /NRST_S6: track 0.00 -> 40.9 mm
- net /NRST_S1: track 0.00 -> 30.3 mm
- net /NRST_S5: track 0.00 -> 29.5 mm, vias 0 -> 2
- net /CC1: track 0.00 -> 26.0 mm, vias 0 -> 1
- net /D-: track 0.00 -> 23.7 mm
- net /D+: track 0.00 -> 23.6 mm
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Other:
- board text added: "Compute Module"

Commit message: first commit: removed 1 MCU
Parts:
- removed C22, C23: 100nF, Capacitor_SMD:C_0603_1608Metric
- removed S9_GP0, S9_GP1, S9_GP10, S9_GP11, S9_GP12, S9_GP13, S9_GP2, S9_GP3, S9_GP4, S9_GP5, S9_GP6, S9_GP7, S9_GP8, S9_GP9: ~, TestPoint:TestPoint_Pad_D1.0mm
- removed TP9: SWIO_N9, TestPoint:TestPoint_Pad_D1.5mm
- removed U9: CH32V006F8P6, Package_SO:TSSOP-20_4.4x6.5mm_P0.65mm
- moved S1_GP0 29.9 mm to (117.3, 112.3)
- moved S1_GP2 29.9 mm to (118.6, 117.4)
- moved S1_GP5 29.9 mm to (116.1, 117.4)
- moved S1_GP7 29.9 mm to (114.8, 112.3)
- moved S2_GP10 29.9 mm to (105.9, 112.3)
- moved S2_GP3 29.9 mm to (108.5, 112.3)
- moved S2_GP5 29.9 mm to (109.7, 117.4)
- moved S2_GP8 29.9 mm to (107.2, 117.4)
- moved S3_GP10 29.9 mm to (97.0, 112.3)
- moved S3_GP3 29.9 mm to (99.6, 112.3)
- moved S3_GP5 29.9 mm to (100.8, 117.4)
- moved S3_GP8 29.9 mm to (98.3, 117.4)
- moved S4_GP1 29.9 mm to (89.4, 107.2)
- moved S4_GP10 29.9 mm to (88.1, 112.3)
- moved S4_GP3 29.9 mm to (90.7, 112.3)
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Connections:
- M1 pad 11: /NRST_S6 -> Net-(M1-PA5)
- M1 pad 12: /NRST_S7 -> /NRST_S6
- M1 pad 13: /NRST_S8 -> /NRST_S7
- M1 pad 14: /NRST_S9 -> /NRST_S8
- R11 pad 1: Net-(U9-PD3) -> Net-(M1-PA5)
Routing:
- net +3.3V: track 201.7 -> 0.00 mm, vias 14 -> 0
- net /BUS_MISO: track 148.0 -> 0.00 mm, vias 6 -> 0
- net /BUS_MOSI: track 138.1 -> 0.00 mm, vias 15 -> 0
- net /NRST_S8: track 66.7 -> 0.00 mm, vias 2 -> 0
- net /NRST_S7: track 65.4 -> 0.00 mm
- net /NRST_S9: track 63.7 -> 0.00 mm, vias 2 -> 0
- net /NRST_S4: track 46.0 -> 0.00 mm, vias 2 -> 0
- net +5V: track 42.6 -> 0.00 mm, vias 3 -> 0
- net /NRST_MASTER: track 41.0 -> 0.00 mm, vias 2 -> 0
- net /NRST_S6: track 40.9 -> 0.00 mm
- net /NRST_S1: track 30.3 -> 0.00 mm
- net /NRST_S5: track 29.5 -> 0.00 mm, vias 2 -> 0
- net /CC1: track 26.0 -> 0.00 mm, vias 1 -> 0
- net /D-: track 23.7 -> 0.00 mm
- net /D+: track 23.6 -> 0.00 mm
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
